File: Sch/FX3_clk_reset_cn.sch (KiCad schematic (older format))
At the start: 18 parts

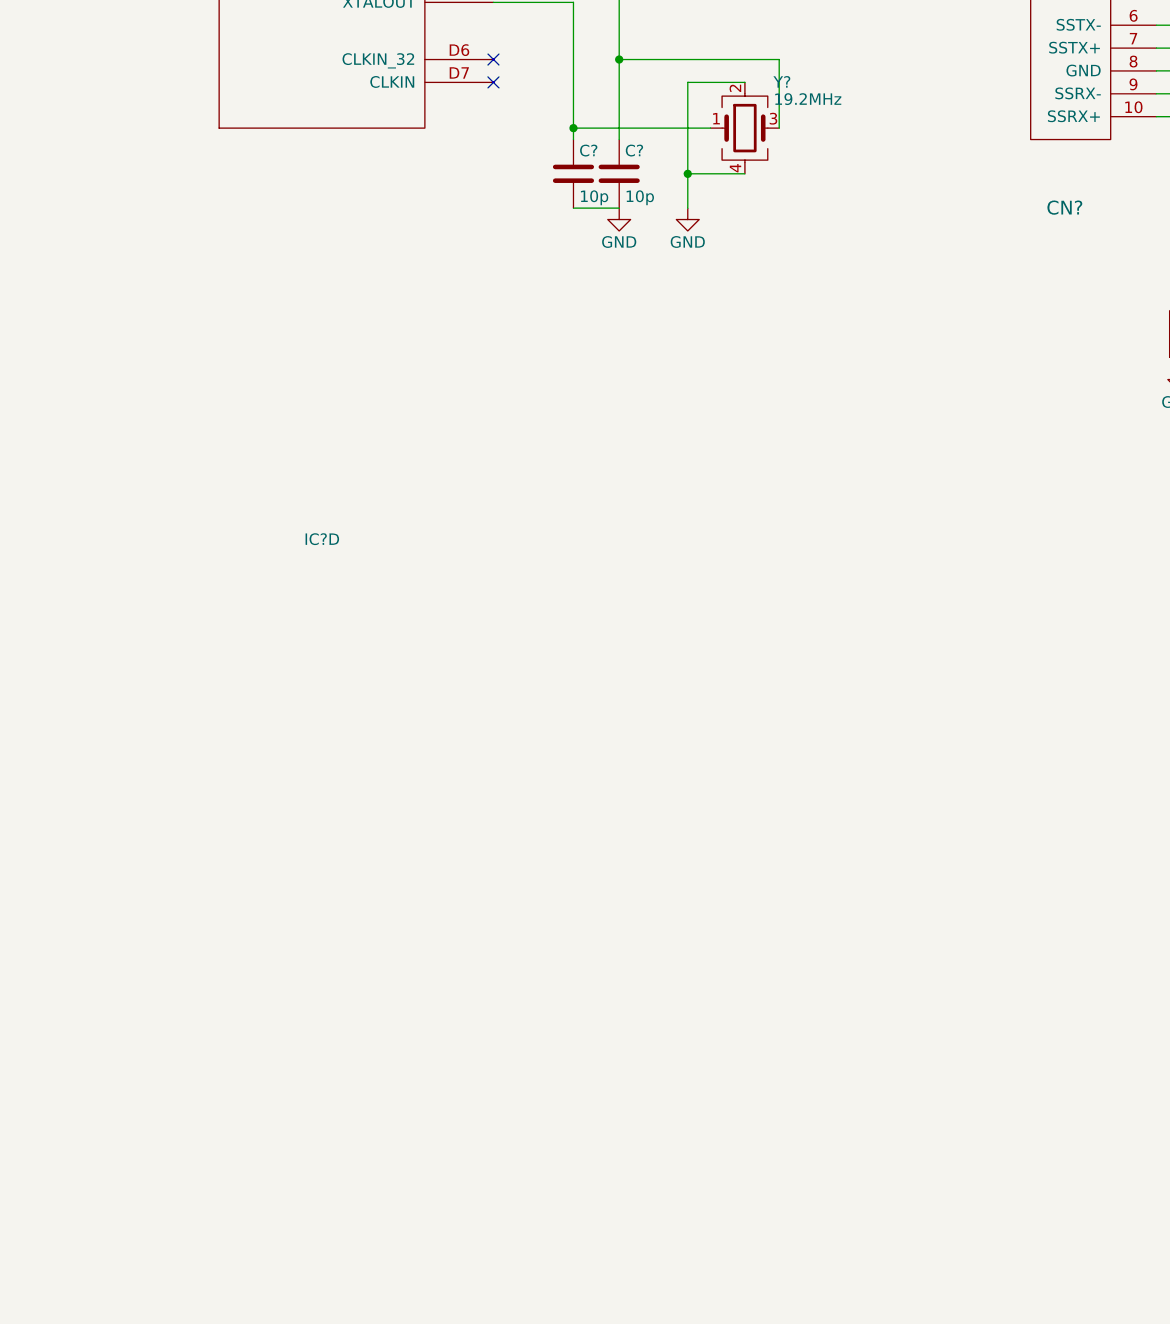
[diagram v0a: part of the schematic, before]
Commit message: FX3 clock,reset,cn
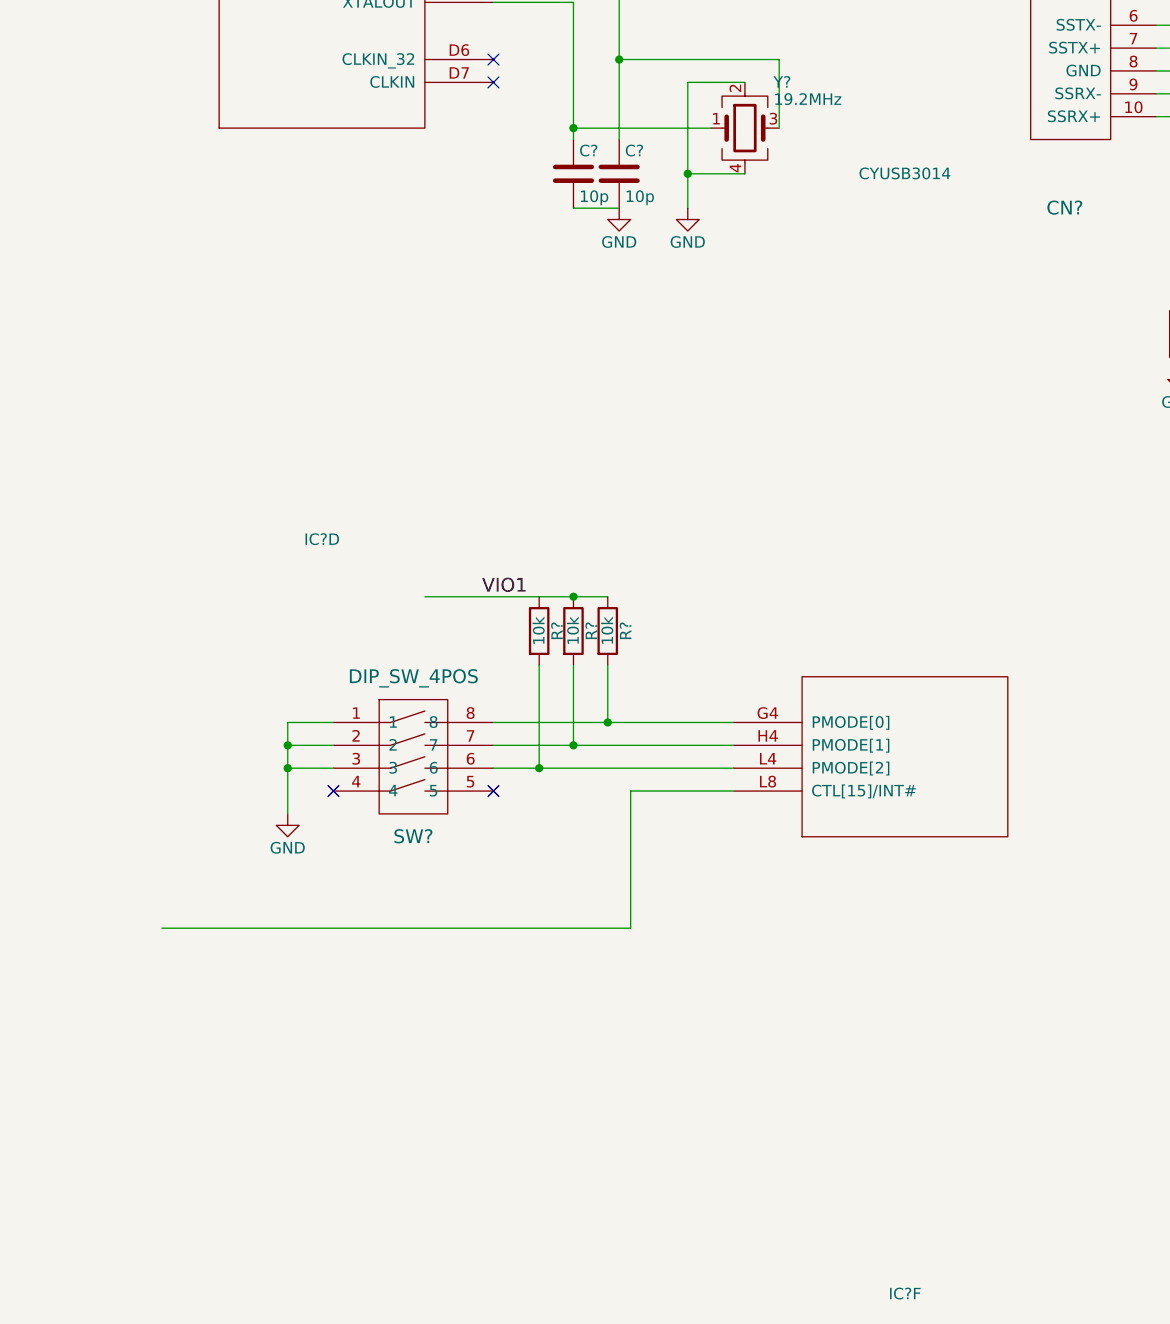
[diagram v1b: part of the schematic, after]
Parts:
- added IC?: CYUSB3014, MODULE, symbol CYUSB3014
- added R? (x3): 10k, symbol R
- added SW?: DIP_SW_4POS, symbol DIP_SW_4POS
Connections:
- net labels added: VIO1
- wire segments 53 -> 67
- no-connect marks 3 -> 5
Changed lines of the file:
@@
 	1    0    0    -1
 $EndComp
-Wire Wire Line
-	5100 3650 4850 3650
-Wire Wire Line
-	4850 3650 4850 4200
-Wire Wire Line
-	5100 4050 4850 4050
-Connection ~ 4850 4050
-Wire Wire Line
-	4950 3850 4350 3850
-Wire Wire Line
-	4350 3300 4350 3900
-Wire Wire Line
-	5250 3850 5250 3550
-Wire Wire Line
-	5250 3550 4550 3550
-Wire Wire Line
-	4550 3200 4550 3900
-Wire Wire Line
-	4350 4200 4550 4200
-Connection ~ 4350 3850
-Connection ~ 4550 3550
-Wire Wire Line
-	1350 3450 1650 3450
-Connection ~ 1500 3450
-Wire Wire Line
-	1650 3150 2500 3150
-Wire Wire Line
-	2500 3050 1500 3050
-Wire Wire Line
-	1500 3050 1500 3150
-Wire Wire Line
-	2500 2950 1350 2950
-Wire Wire Line
-	1350 2950 1350 3150
-Wire Wire Line
-	9050 3400 8700 3400
-Wire Wire Line
-	9050 3500 8700 3500
-Wire Wire Line
-	6900 3400 7600 3400
-Wire Wire Line
-	6900 3500 7600 3500
-Wire Wire Line
-	6900 3250 7250 3250
-Wire Wire Line
-	7250 3250 7250 4450
-Wire Wire Line
-	6900 3600 7250 3600
-Connection ~ 7250 3600
-Wire Wire Line
-	6900 3700 7350 3700
-Wire Wire Line
-	7350 3700 7350 3100
-Wire Wire Line
-	7350 3100 7600 3100
-Wire Wire Line
-	8400 3100 8900 3100
-Wire Wire Line
-	8900 3100 8900 3200
-Wire Wire Line
-	8900 3200 9050 3200
-Wire Wire Line
-	8400 3200 8800 3200
-Wire Wire Line
-	8800 3200 8800 3300
-Wire Wire Line
-	8800 3300 9050 3300
-Wire Wire Line
-	6900 3800 7450 3800
-Wire Wire Line
-	7450 3800 7450 3200
-Wire Wire Line
-	7450 3200 7600 3200
-Wire Wire Line
-	7600 3300 7600 4350
-Wire Wire Line
-	7250 4350 8400 4350
-Connection ~ 7250 4350
-Wire Wire Line
-	8400 4350 8400 3300
-Connection ~ 7600 4350
-Wire Wire Line
-	4000 3300 4350 3300
-Wire Wire Line
-	4000 3200 4550 3200
-Wire Wire Line
-	8700 3600 9050 3600
-Wire Wire Line
-	8700 3700 9050 3700
-Wire Wire Line
-	6900 3000 7200 3000
-Wire Wire Line
-	6900 2900 7200 2900
-Wire Wire Line
-	8700 3700 8700 4600
-Wire Wire Line
-	8950 4600 8950 3600
-Connection ~ 8950 3600
-Wire Wire Line
-	9050 3900 7800 3900
-Wire Wire Line
-	7800 3900 7800 4600
-Wire Wire Line
-	9050 4000 8000 4000
-Wire Wire Line
-	8000 4000 8000 4600
-Wire Wire Line
-	9050 4100 8250 4100
-Wire Wire Line
-	8250 4100 8250 4600
 $Comp
 L GND #PWR?
@@
 	1    0    0    -1
 $EndComp
+$Comp
+L CYUSB3014 IC?
+U 6 1 58A06F9C
+P 5800 6600
+F 0 "IC?" H 5800 4250 50  0000 C CNN
+F 1 "CYUSB3014" H 5800 9150 50  0000 C CNN
+F 2 "MODULE" H 5750 8900 50  0001 C CNN
+F 3 "DOCUMENTATION" H 5800 9050 50  0001 C CNN
+	6    5800 6600
+	1    0    0    -1
+$EndComp
+Wire Wire Line
+	5100 3650 4850 3650
+Wire Wire Line
+	4850 3650 4850 4200
+Wire Wire Line
+	5100 4050 4850 4050
+Connection ~ 4850 4050
+Wire Wire Line
+	4950 3850 4350 3850
+Wire Wire Line
+	4350 3300 4350 3900
+Wire Wire Line
+	5250 3850 5250 3550
+Wire Wire Line
+	5250 3550 4550 3550
+Wire Wire Line
+	4550 3200 4550 3900
+Wire Wire Line
+	4350 4200 4550 4200
+Connection ~ 4350 3850
+Connection ~ 4550 3550
+Wire Wire Line
+	1350 3450 1650 3450
+Connection ~ 1500 3450
+Wire Wire Line
+	1650 3150 2500 3150
+Wire Wire Line
+	2500 3050 1500 3050
+Wire Wire Line
+	1500 3050 1500 3150
+Wire Wire Line
+	2500 2950 1350 2950
+Wire Wire Line
+	1350 2950 1350 3150
+Wire Wire Line
+	9050 3400 8700 3400
+Wire Wire Line
+	9050 3500 8700 3500
+Wire Wire Line
+	6900 3400 7600 3400
+Wire Wire Line
+	6900 3500 7600 3500
+Wire Wire Line
+	6900 3250 7250 3250
+Wire Wire Line
+	7250 3250 7250 4450
+Wire Wire Line
+	6900 3600 7250 3600
+Connection ~ 7250 3600
+Wire Wire Line
+	6900 3700 7350 3700
+Wire Wire Line
+	7350 3700 7350 3100
+Wire Wire Line
+	7350 3100 7600 3100
+Wire Wire Line
+	8400 3100 8900 3100
+Wire Wire Line
+	8900 3100 8900 3200
+Wire Wire Line
+	8900 3200 9050 3200
+Wire Wire Line
+	8400 3200 8800 3200
+Wire Wire Line
+	8800 3200 8800 3300
+Wire Wire Line
+	8800 3300 9050 3300
+Wire Wire Line
+	6900 3800 7450 3800
+Wire Wire Line
+	7450 3800 7450 3200
+Wire Wire Line
+	7450 3200 7600 3200
+Wire Wire Line
+	7600 3300 7600 4350
+Wire Wire Line
+	7250 4350 8400 4350
+Connection ~ 7250 4350
+Wire Wire Line
+	8400 4350 8400 3300
+Connection ~ 7600 4350
+Wire Wire Line
+	4000 3300 4350 3300
+Wire Wire Line
+	4000 3200 4550 3200
+Wire Wire Line
+	8700 3600 9050 3600
+Wire Wire Line
+	8700 3700 9050 3700
+Wire Wire Line
+	6900 3000 7200 3000
+Wire Wire Line
+	6900 2900 7200 2900
+Wire Wire Line
+	8700 3700 8700 4600
+Wire Wire Line
+	8950 4600 8950 3600
+Connection ~ 8950 3600
+Wire Wire Line
+	9050 3900 7800 3900
+Wire Wire Line
+	7800 3900 7800 4600
+Wire Wire Line
+	9050 4000 8000 4000
+Wire Wire Line
+	8000 4000 8000 4600
+Wire Wire Line
+	9050 4100 8250 4100
+Wire Wire Line
+	8250 4100 8250 4600
 Wire Wire Line
 	6900 3100 7000 3100
 Wire Wire Line
 	7000 3100 7000 4600
+Wire Wire Line
+	3700 5900 4500 5900
+Text Label 3950 5900 0    60   ~ 0
+VIO1
+$Comp
+L R R?
+U 1 1 58A073A6
+P 4200 6050
+F 0 "R?" V 4280 6050 50  0000 C CNN
+F 1 "10k" V 4200 6050 50  0000 C CNN
+F 2 "" V 4130 6050 50  0000 C CNN
+F 3 "" H 4200 6050 50  0000 C CNN
+	1    4200 6050
+	1    0    0    -1
+$EndComp
+$Comp
+L R R?
+U 1 1 58A07409
+P 4350 6050
+F 0 "R?" V 4430 6050 50  0000 C CNN
+F 1 "10k" V 4350 6050 50  0000 C CNN
+F 2 "" V 4280 6050 50  0000 C CNN
+F 3 "" H 4350 6050 50  0000 C CNN
+	1    4350 6050
+	1    0    0    -1
+$EndComp
+$Comp
+L R R?
+U 1 1 58A07452
+P 4500 6050
+F 0 "R?" V 4580 6050 50  0000 C CNN
+F 1 "10k" V 4500 6050 50  0000 C CNN
+F 2 "" V 4430 6050 50  0000 C CNN
+F 3 "" H 4500 6050 50  0000 C CNN
+	1    4500 6050
+	1    0    0    -1
+$EndComp
+Connection ~ 4350 5900
+Wire Wire Line
+	4500 6200 4500 6450
+Wire Wire Line
+	4000 6450 5050 6450
+Wire Wire Line
+	4350 6200 4350 6550
+Wire Wire Line
+	4000 6550 5050 6550
+Wire Wire Line
+	4200 6200 4200 6650
+Wire Wire Line
+	4000 6650 5050 6650
+$Comp
+L GND #PWR?
+U 1 1 58A077E4
+P 3100 6850
+F 0 "#PWR?" H 3100 6600 50  0001 C CNN
+F 1 "GND" H 3100 6700 50  0000 C CNN
+F 2 "" H 3100 6850 50  0000 C CNN
+F 3 "" H 3100 6850 50  0000 C CNN
+	1    3100 6850
+	1    0    0    -1
+$EndComp
+$Comp
+L DIP_SW_4POS SW?
+U 1 1 58A07985
+P 3650 6600
+F 0 "SW?" H 3650 6250 60  0000 C CNN
+F 1 "DIP_SW_4POS" H 3650 6950 60  0000 C CNN
+F 2 "" H 3750 6450 60  0001 C CNN
+F 3 "" H 3750 6450 60  0001 C CNN
+	1    3650 6600
+	1    0    0    -1
+$EndComp
+NoConn ~ 3300 6750
+Wire Wire Line
+	3300 6450 3100 6450
+Wire Wire Line
+	3100 6450 3100 6850
+Wire Wire Line
+	3300 6550 3100 6550
+Connection ~ 3100 6550
+Wire Wire Line
+	3300 6650 3100 6650
+Connection ~ 3100 6650
+Connection ~ 4500 6450
+Connection ~ 4350 6550
+Connection ~ 4200 6650
+NoConn ~ 4000 6750
+Wire Wire Line
+	5050 6750 4600 6750
+Wire Wire Line
+	4600 6750 4600 7350
+Wire Wire Line
+	4600 7350 2550 7350
 $EndSCHEMATC
